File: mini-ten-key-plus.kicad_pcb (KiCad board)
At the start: 2 copper layers, 76.2 x 95.3 mm, 50 parts, among them SW0 SW_Push, U0 ProMicro

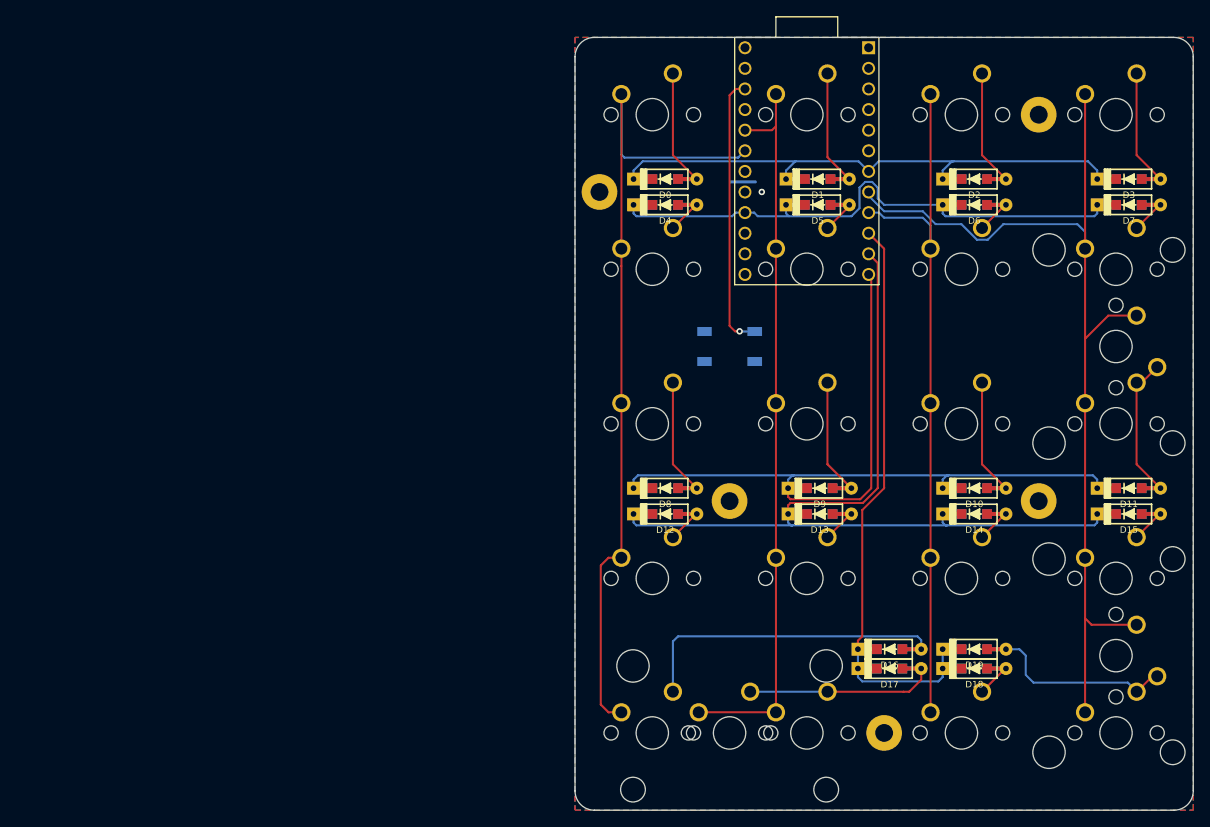
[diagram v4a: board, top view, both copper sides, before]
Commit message: Added extra column of keys on the left side
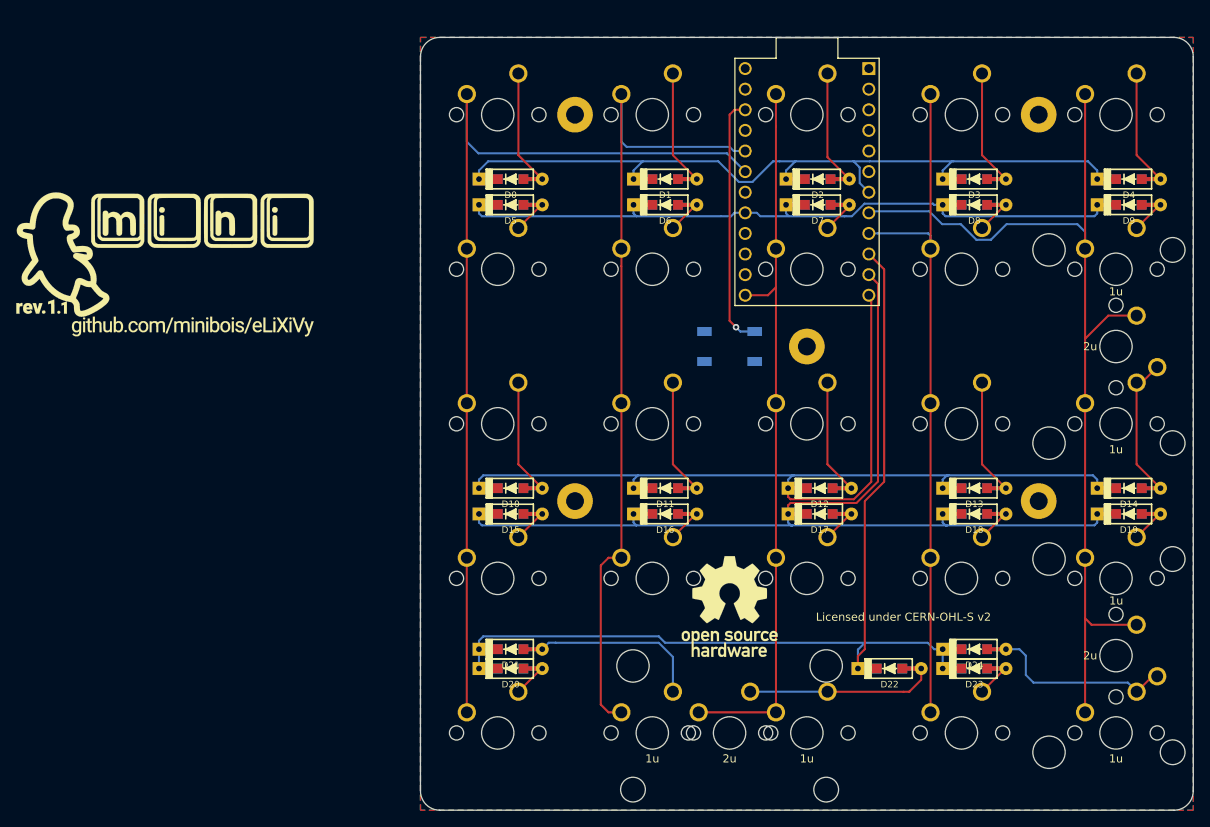
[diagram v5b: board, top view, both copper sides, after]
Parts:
- removed the D8 at (218.3, 124.6)
- added D0: D_Small, mini-general-tweaks:D_SOD123_axial-dual, F.Cu at (199.2, 86.5)
- added D10: D_Small, mini-general-tweaks:D_SOD123_axial-dual, F.Cu at (199.2, 124.6)
- added D11: D_Small, mini-general-tweaks:D_SOD123_axial-dual, F.Cu at (218.3, 124.6)
- added D15: D_Small, mini-general-tweaks:D_SOD123_axial-dual, F.Cu at (199.2, 127.8)
- added D20: D_Small, mini-general-tweaks:D_SOD123_axial-dual, F.Cu at (199.2, 146.8)
- added D5: D_Small, mini-general-tweaks:D_SOD123_axial-dual, F.Cu at (199.2, 89.7)
- added LO0: mini-tkp-SilkScreen, mini-Logos:eLiXiVy-rev1.1-SilkScreen, F.Cu at (156.7, 97.1)
- added LO1: mini-tkp-Mask, mini-Logos:eLiXiVy-rev1.1-Mask, F.Cu at (156.7, 97.1)
- added LO2: OSHW-Logo, mini-Logos:OSHW-Logo, F.Cu at (226.2, 139.2)
- added LO3: OSHW-Text, mini-Logos:OSHW-Text, F.Cu at (254.8, 162.7)
- added MX0: MX-NoLED, mini-MX-Tweaks:MXOnly-1U-NoLED_tweak, F.Cu at (197.6, 78.6)
- added MX10: MX-NoLED, mini-MX-Tweaks:MXOnly-1U-NoLED_tweak, F.Cu at (197.6, 116.7)
- added MX15: MX-NoLED, mini-MX-Tweaks:MXOnly-1U-NoLED_tweak, F.Cu at (197.6, 135.7)
- added MX20: MX-NoLED, mini-MX-Tweaks:MXOnly-1U-NoLED_tweak, F.Cu at (197.6, 154.8)
- added MX5: MX-NoLED, mini-MX-Tweaks:MXOnly-1U-NoLED_tweak, F.Cu at (197.6, 97.6)
- moved H3 48.6 mm to (235.7, 107.2)
- moved D21 46.7 mm to (199.2, 144.5)
- moved H1 19.1 mm to (207.2, 126.2)
- moved H4 9.99 mm to (207.2, 78.6)
- moved U0 2.57 mm to (235.8, 86.9)
- renumbered D0 to D1, D9 to D12, D10 to D13, D11 to D14, D12 to D16, D13 to D17, D14 to D18, D15 to D19, D1 to D2, D16 to D21, D17 to D22, D18 to D23, D19 to D24, D2 to D3, D3 to D4, D4 to D6, D5 to D7, D6 to D8, D7 to D9, MX0 to MX1, MX8 to MX11, MX9 to MX12, MX10 to MX13, MX11 to MX14, MX12 to MX16, MX13 to MX17, MX14 to MX18, MX15 to MX19, MX1 to MX2, MX16 to MX21, MX17 to MX22, MX18 to MX23, MX19 to MX24, MX20 to MX25, MX21 to MX26, MX22 to MX27, MX2 to MX3, MX3 to MX4, MX4 to MX6, MX5 to MX7, MX6 to MX8, MX7 to MX9
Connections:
- MX1 pad 1: COL0 -> COL1
- MX11 pad 1: COL0 -> COL1
- MX12 pad 1: COL1 -> COL2
- MX13 pad 1: COL2 -> COL3
- MX14 pad 1: COL3 -> COL4
- MX16 pad 1: COL0 -> COL1
- MX17 pad 1: COL1 -> COL2
- MX18 pad 1: COL2 -> COL3
- MX19 pad 1: COL3 -> COL4
- MX2 pad 1: COL1 -> COL2
- MX21 pad 1: COL0 -> COL1
- MX22 pad 1: COL1 -> COL2
- MX23 pad 1: COL2 -> COL3
- MX24 pad 1: COL3 -> COL4
- MX25 pad 1: COL3 -> COL4
- MX26 pad 1: COL1 -> COL2
- MX27 pad 1: COL3 -> COL4
- MX3 pad 1: COL2 -> COL3
- MX4 pad 1: COL3 -> COL4
- MX6 pad 1: COL0 -> COL1
- MX7 pad 1: COL1 -> COL2
- MX8 pad 1: COL2 -> COL3
- MX9 pad 1: COL3 -> COL4
- U0 pad 13: Net-(U0-Pad13) -> COL2
- U0 pad 16: ROW1 -> Net-(U0-Pad16)
- U0 pad 17: Net-(U0-Pad17) -> ROW1
- U0 pad 8: COL3 -> COL4
- U0 pad 9: COL2 -> COL3
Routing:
- net COL4: track 0.00 -> 121.9 mm
- net ROW4: track 71.2 -> 120.6 mm
- net COL3: track 123.4 -> 85.5 mm
- net ROW0: track 66.8 -> 94.3 mm
- net ROW3: track 105.4 -> 123.4 mm
- net ROW2: track 102.2 -> 120.0 mm
- net Net-(D21-Pad2): track 38.4 -> 21.4 mm
- net ROW1: track 67.9 -> 84.1 mm
- net COL0: track 103.4 -> 117.9 mm
- net Net-(D10-Pad2): track 0.00 -> 14.2 mm
- net Net-(D0-Pad2): track 0.00 -> 14.2 mm
- net COL1: track 89.7 -> 101.8 mm
- net Net-(D5-Pad2): track 0.00 -> 4.13 mm
- net Net-(D15-Pad2): track 0.00 -> 4.13 mm
- net Net-(D20-Pad2): track 0.00 -> 4.13 mm
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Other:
- board size 76.2 x 95.3 mm -> 95.2 x 95.2 mm
- board text added: "1u"
- board text added: "2u"

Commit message: Made gerber files
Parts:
- added RE0: Rotary_Encoder_Switch, mini-general-tweaks:RotaryEncoder_Alps_EC11E-Switch-Vertical-EDIT, F.Cu at (195.1, 86.1)
- LO0: footprint mini-Logos:eLiXiVy-rev1.1-SilkScreen -> mini-Logos:mini-TKP-BSilk
- LO1: footprint mini-Logos:eLiXiVy-rev1.1-Mask -> mini-Logos:mini-TKP-BMask
- LO2: moved to B.Cu
- moved LO0 56.9 mm to (213.0, 105.2)
- moved LO1 56.9 mm to (213.0, 105.2)
- moved RESET 19.1 mm to (245.3, 107.2)
- moved D0 7.94 mm to (207.2, 86.5)
- moved D5 7.94 mm to (207.2, 89.7)
- moved H0 3.97 mm to (264.3, 74.6)
- moved H4 3.97 mm to (207.2, 74.6)
- moved D21 0.79 mm to (199.2, 143.7)
- moved D24 0.79 mm to (256.4, 143.7)
- turned LO2 to 180 degrees
- renumbered SW0 to RESET
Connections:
- net Net-(D0-Pad2) renamed ROW0_RE
- U0 pad 16: Net-(U0-Pad16) -> ROW1
- U0 pad 17: ROW1 -> RE+
- U0 pad 18: Net-(U0-Pad18) -> RE-
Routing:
- net RE+: track 0.00 -> 35.6 mm
- net RE-: track 0.00 -> 29.6 mm
- net RESET: track 31.2 -> 50.3 mm
- net ROW0_RE: track 14.2 -> 24.7 mm
- net ROW0: track 94.3 -> 85.0 mm
- net Net-(D5-Pad2): track 4.13 -> 12.1 mm
- net ROW1: track 84.1 -> 78.4 mm
- net COL0: track 117.9 -> 123.6 mm
- net ROW4: track 120.6 -> 122.7 mm
- net Net-(D24-Pad2): track 23.0 -> 23.8 mm

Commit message: Added additional info to PCB/Schematic and added PCB/Schematic PDF
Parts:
- moved D12 166.4 mm to (80.2, 69.8)
- moved D13 166.4 mm to (99.2, 69.8)
- moved D17 166.4 mm to (80.2, 73.0)
- moved D18 166.4 mm to (99.2, 73.0)
- moved D23 166.4 mm to (99.2, 92.1)
- moved D24 166.4 mm to (99.2, 88.9)
- moved D3 166.4 mm to (99.2, 31.8)
- moved D8 166.4 mm to (99.2, 34.9)
- moved H0 166.4 mm to (107.2, 19.8)
- moved H2 166.4 mm to (107.2, 71.4)
- moved H3 166.4 mm to (78.6, 52.4)
- moved LO0 166.4 mm to (55.8, 50.4)
- moved LO1 166.4 mm to (55.8, 50.4)
- moved MX0 166.4 mm to (40.5, 23.8)
- moved MX10 166.4 mm to (40.5, 61.9)
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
